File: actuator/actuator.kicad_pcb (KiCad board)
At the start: 2 copper layers, 23.2 x 21 mm, 13 parts, among them J1 IN, J2 OUT1, J3 OUT2, J4 SWD, M1 DSOS-0416-24D, Q1 2N7002, U1 STM32G030F6Px

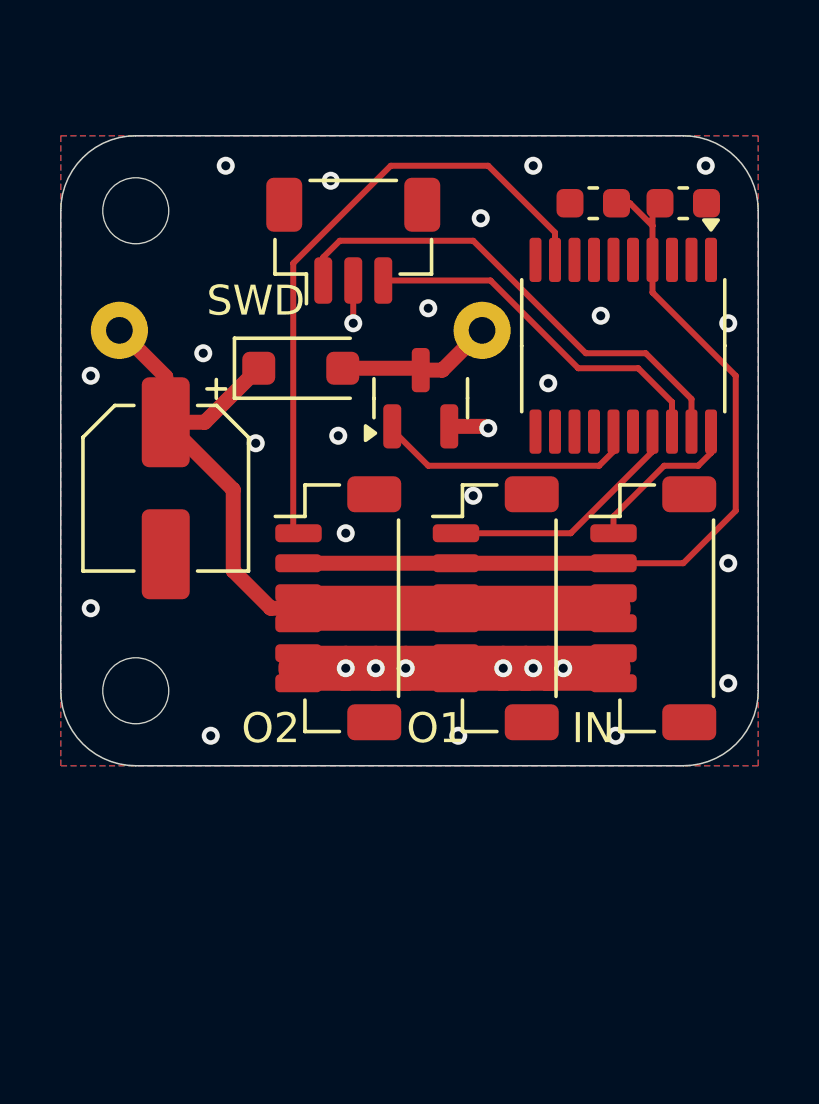
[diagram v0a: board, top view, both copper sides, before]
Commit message: new version w/ Chonky nano-fit connectors
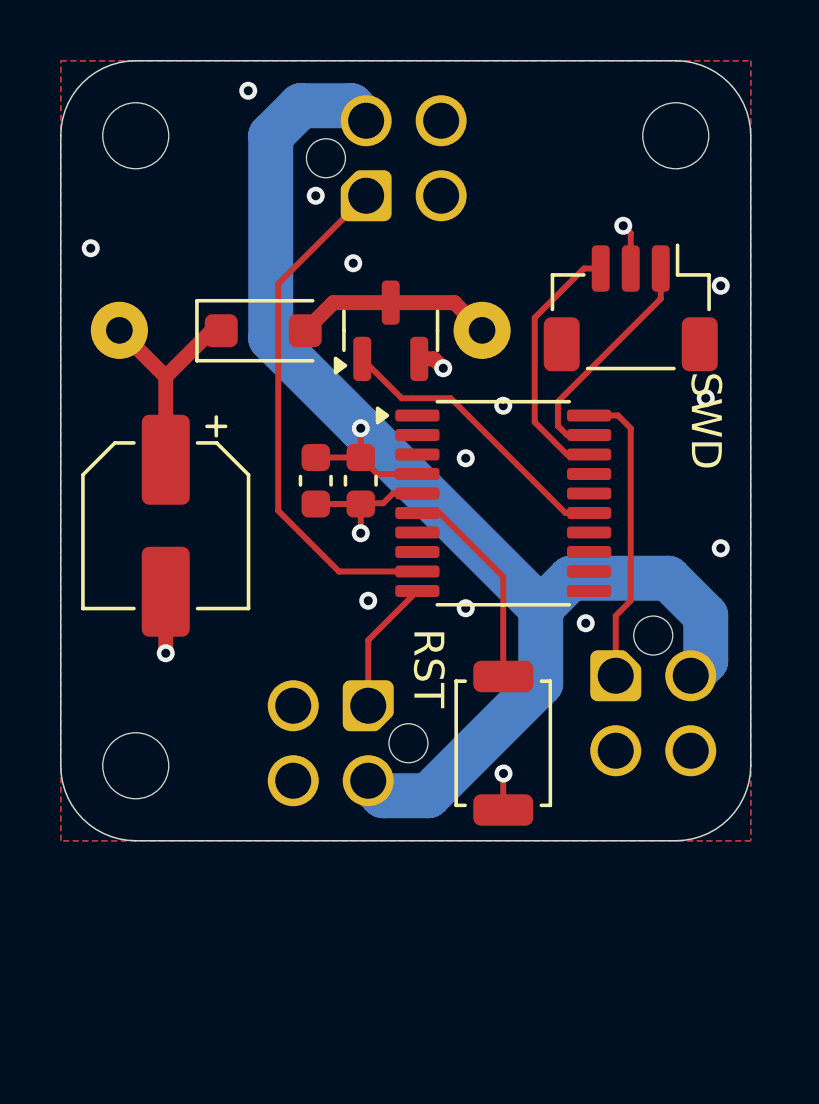
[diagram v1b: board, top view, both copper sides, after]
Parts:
- added REF**: MountingHole_2.2mm_M2, MountingHole:MountingHole_2.2mm_M2, F.Cu at (119.2, 75.2)
- added SW1: RESET, custom:SW_Push_SPST_TS-1088, F.Cu at (113.4, 95.5)
- J1, J2, J3: footprint Connector_JST:JST_SH_BM06B-SRSS-TB_1x06-1MP_P1.00mm_Vertical -> custom:Molex_Nano-Fit_105310-xx04_2x02_P2.50mm_Vertical; moved to B.Cu
- moved C2 14.2 mm to (108.7, 86.7), turned to -90 degrees
- moved J3 13.8 mm to (108.9, 77.2), turned to 0 degrees
- moved C3 13.1 mm to (107.2, 86.7), turned to -90 degrees
- moved J1 10.0 mm to (108.9, 94.2), turned to 180 degrees
- moved J4 9.52 mm to (117.7, 81.0), turned to 180 degrees
- moved U1 6.60 mm to (113.4, 87.5), turned to 0 degrees
- moved J2 4.59 mm to (117.2, 93.2)
- moved REF** 2.50 mm to (101.2, 75.2)
- moved REF** 2.50 mm to (101.2, 96.2)
- moved Q1 2.46 mm to (109.7, 81.7)
- moved D1 1.77 mm to (105.4, 81.7)
- moved C1 1.25 mm to (102.2, 88.2)
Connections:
- J1 pad 4: +48V -> GND
- J2 pad 4: +48V -> GND
- J3 pad 4: +48V -> GND
- U1 pad 10: unconnected-(U1-PA3-Pad10) -> /RX
- U1 pad 17: /RX -> unconnected-(U1-PA10/PA12-Pad17)
- U1 pad 6: unconnected-(U1-NRST-Pad6) -> Net-(SW1-B)
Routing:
- net +48V: track 26.4 -> 7.46 mm
- net +3.3V: track 28.3 -> 46.5 mm, vias 0 -> 1
- net /SWCLK: track 16.6 -> 7.83 mm
- net Net-(SW1-B): track 0.00 -> 7.07 mm
- net /TX1: track 5.40 -> 10.0 mm
- net /RX: track 8.34 -> 4.50 mm
- net /TX2: track 21.0 -> 17.2 mm
- net /SWDIO: track 12.3 -> 8.62 mm
- net GND: track 13.0 -> 10.2 mm, vias 29 -> 17
- net Net-(D1-A): track 5.22 -> 6.77 mm
- net /PWM: track 8.84 -> 9.69 mm
- added copper zone on In1.Cu, net +48V
- added copper zone on In2.Cu, net GND
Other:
- board size 23.2 x 21 mm -> 23 x 26 mm
- copper layers 2 -> 4
- board text added: "RST"
- board text added: "Solenoid Haptics rev.3 Sky Bailey"

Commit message: tweaks idk
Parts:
- added REF**: Molex_Nano-Fit_105309-xx03_1x03_P2.50mm_Vertical, Connector_Molex:Molex_Nano-Fit_105309-xx03_1x03_P2.50mm_Vertical, F.Cu at (106.4, 100.7)

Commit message: design review changes
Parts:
- removed the REF** at (106.4, 100.7)
- added R1: 10k, Resistor_SMD:R_0603_1608Metric, F.Cu at (106.9, 84.5)
- added TP1: PWM, custom:TestPoint_RH-5015, F.Cu at (118.7, 87.7)
- added TP2: Solenoid, custom:TestPoint_RH-5015, F.Cu at (114.7, 77.0)
- Q1: value 2N7002 -> FDV301N
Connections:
- net +48V renamed +24V
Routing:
- net Net-(D1-A): track 6.77 -> 11.8 mm
- net /PWM: track 9.69 -> 14.3 mm
- net GND: track 10.2 -> 13.9 mm, vias 17 -> 18
- net /TX1: track 10.0 -> 12.3 mm
- net /TX2: track 17.2 -> 18.0 mm
